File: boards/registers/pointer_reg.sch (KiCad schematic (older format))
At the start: 80 parts

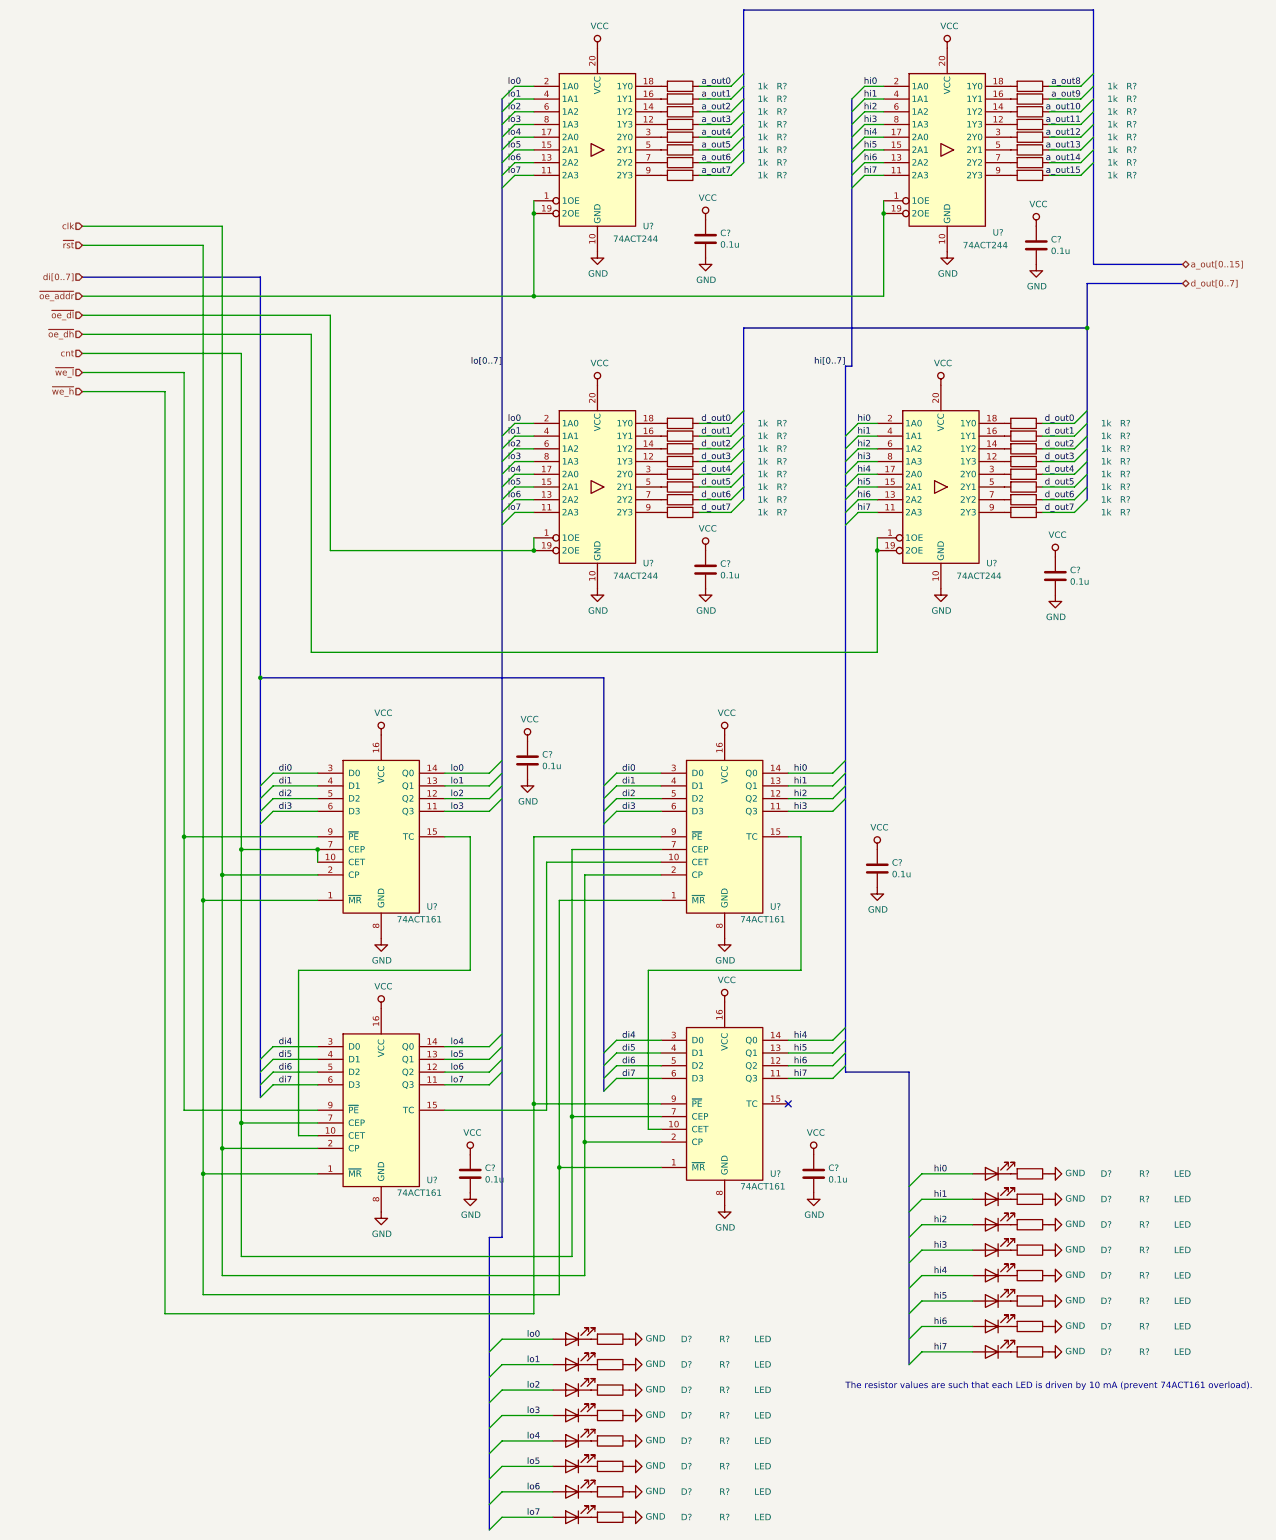
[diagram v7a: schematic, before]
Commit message: Annotated schematics, assigned footprints
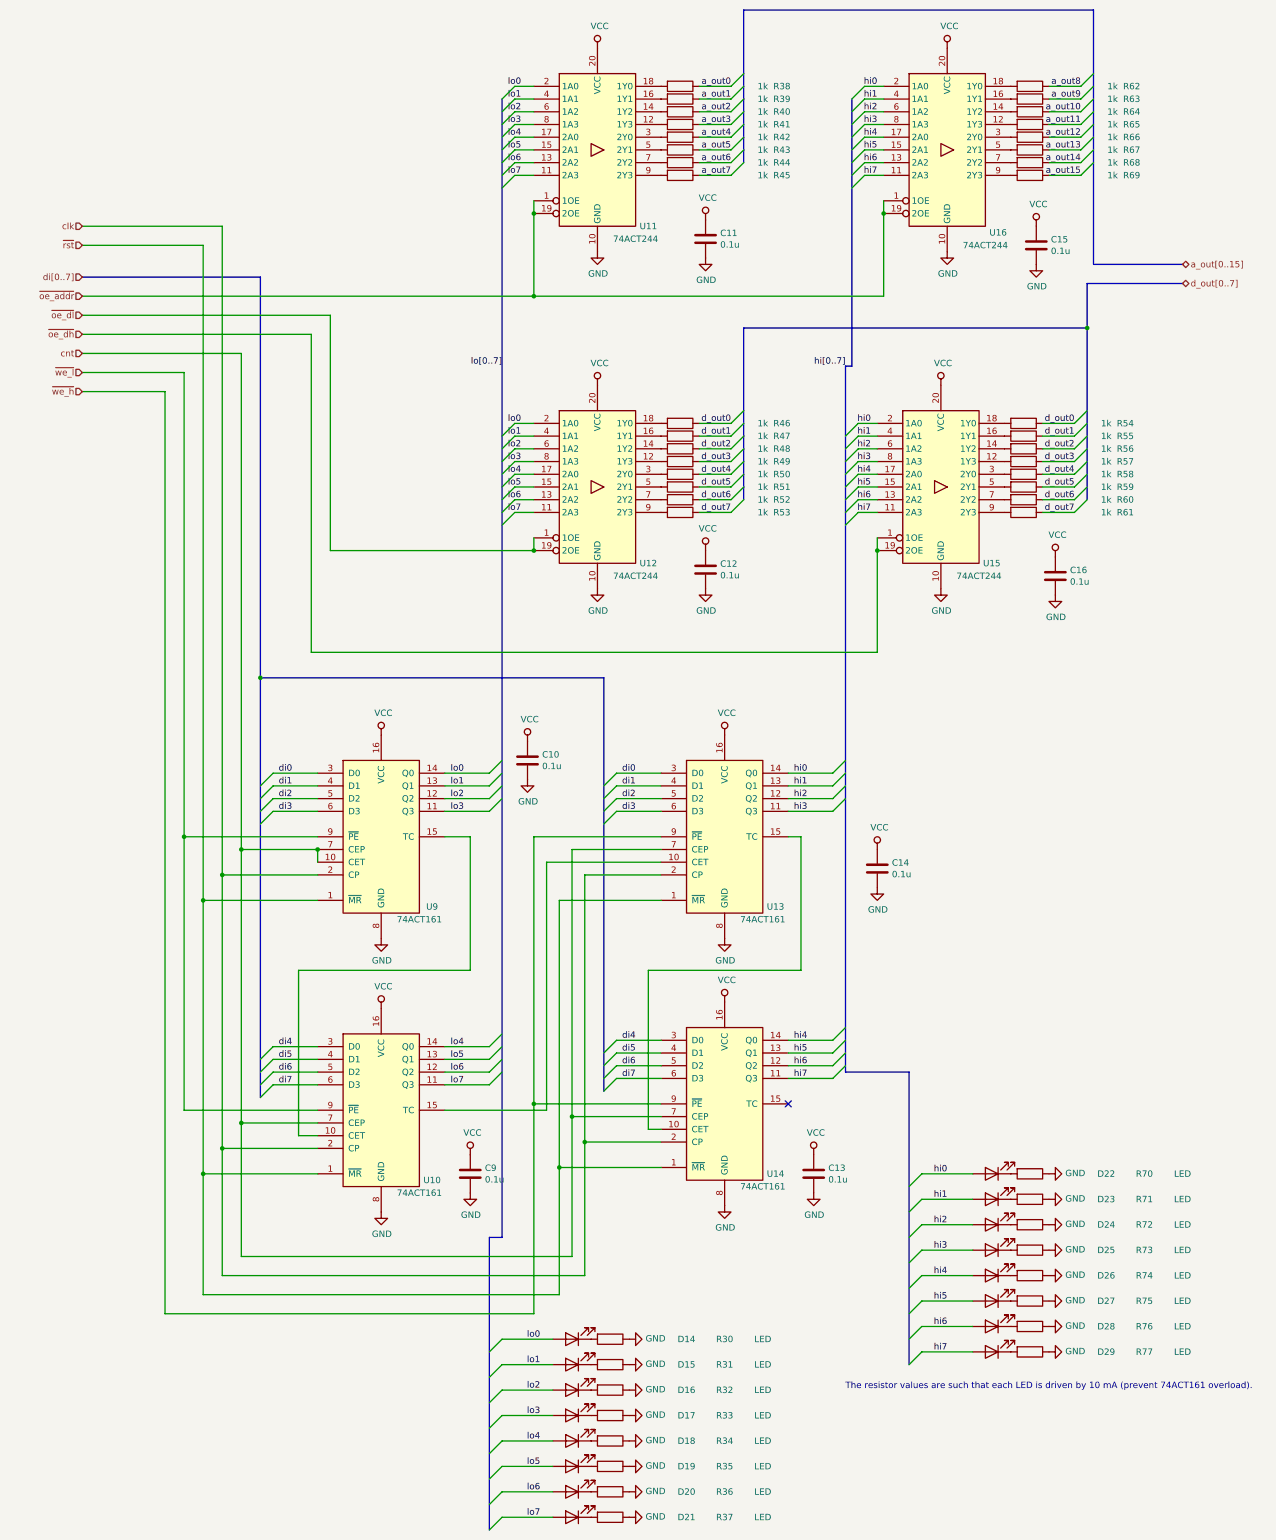
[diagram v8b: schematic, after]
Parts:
- C10, C11, C12, C13, C14, C15, C16, C9: renamed from C?; footprint (none) -> Capacitor_SMD:C_0805_2012Metric
- D14, D15, D16, D17, D18, D19, D20, D21, D22, D23, D24, D25, D26, D27, D28, D29: renamed from D?; footprint (none) -> LED_SMD:LED_0805_2012Metric
- R30, R31, R32, R33, R34, R35, R36, R37, R38, R39, R40, R41, R42, R43, R44, R45, R46, R47, R48, R49, R50, R51, R52, R53, R54, R55, R56, R57, R58, R59, R60, R61, R62, R63, R64, R65, R66, R67, R68, R69, R70, R71, R72, R73, R74, R75, R76, R77: renamed from R?; footprint (none) -> Resistor_SMD:R_0805_2012Metric
- U10, U13, U14, U9: renamed from U?; footprint (none) -> Package_SO:SOIC-16_3.9x9.9mm_P1.27mm
- U11, U12, U15, U16: renamed from U?; footprint (none) -> Package_SO:SO-20_12.8x7.5mm_P1.27mm
